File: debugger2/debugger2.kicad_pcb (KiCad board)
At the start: 2 copper layers, 65 x 30 mm, 63 parts, among them IC1 AT24CS32-SSHM, P1 CONN_01X01, P2 CONN_01X01, P3 USB_OTG, P4 CONN_02X20, P5 CONN_01X02, Q1 Q_PMOS_GSD, Q2 DMMT3906_Dual_PNP, U1 93LC56B, U2 MIC9409x_SC-70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

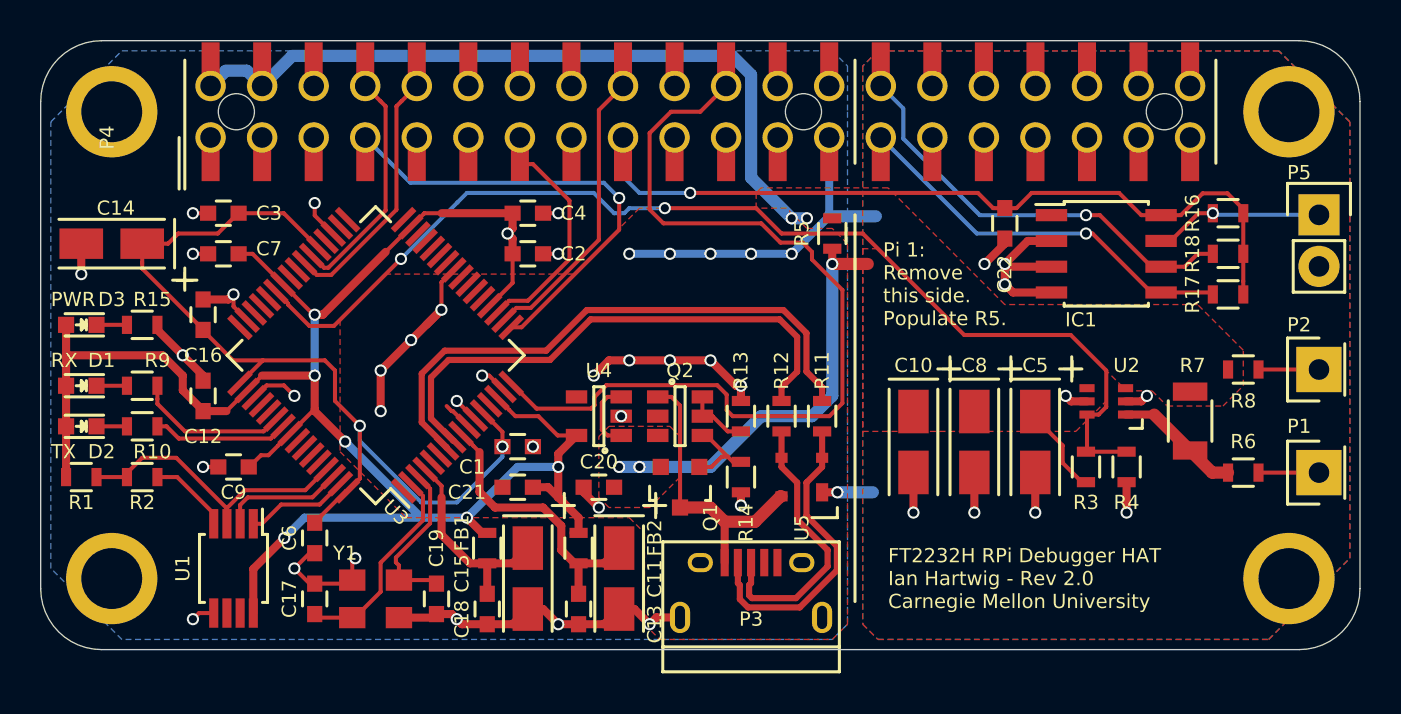
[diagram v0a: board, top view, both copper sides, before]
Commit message: rev 2.1 fixes for UART, JTAG resets, EEPROM packages
* fix UART (FTDI Ch B) RX/TX backwards
* fix GPIO22_TRST floating by connecting to FTDI Ch A. in debugger 1 we pulled up to 3.3V, but this gives us software control of tap reset
* add options to control RPi power (reset) from FTDI Ch A and button. diodes can be left off BOM to disable a source
* add external drain resistor for vbus switch (backpowering from rpi can cause fet drain in the switch to magic smoke)
* add grounding pad for probe clips
* make holes floating so we can use metal standoffs
* make FB1, FB2 be 0805 (not available in 0603)
* make both EEPROMs TSSOP for easier purchasing (but not compatible)
* reroute USB to a shorter path
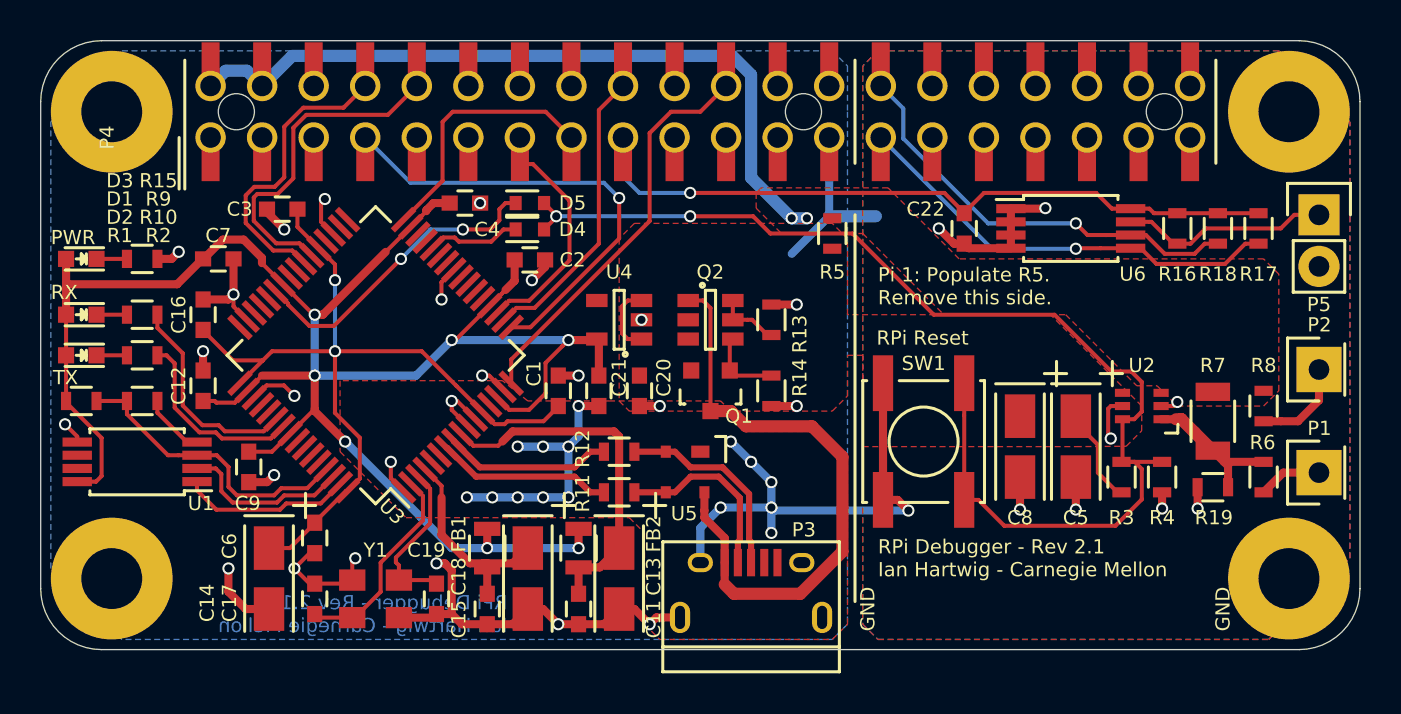
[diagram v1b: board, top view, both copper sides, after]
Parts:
- removed C10: 4.7u, Capacitors_Tantalum_SMD:TantalC_SizeA_EIA-3216_Wave
- removed IC1: AT24CS32-SSHM, Housings_SOIC:SOIC-8_3.9x4.9mm_Pitch1.27mm
- added D4: D_Small, Diodes_SMD:SOD-523, F.Cu at (144.1, 99.3)
- added D5: D_Small, Diodes_SMD:SOD-523, F.Cu at (144.1, 98.0)
- added R19: 10k, Resistors_SMD:R_0603, F.Cu at (177.8, 112.0)
- added SW1: SW_PUSH, Buttons_Switches_SMD:SW_SPST_EVPBF, F.Cu at (163.5, 109.8)
- added U6: AT24CS32-SSHM, Housings_SSOP:TSSOP-8_4.4x3mm_Pitch0.65mm, F.Cu at (170.8, 99.2)
- FB1, FB2: footprint Resistors_SMD:R_0603 -> Resistors_SMD:R_0805
- U1: footprint Housings_SSOP:MSOP-8_3x3mm_Pitch0.65mm -> Housings_SSOP:TSSOP-8_4.4x3mm_Pitch0.65mm
- moved C14 18.2 mm to (131.2, 116.5), turned to 270 degrees
- moved R11 10.7 mm to (148.5, 112.2), turned to 0 degrees
- moved R12 8.19 mm to (148.5, 110.2), turned to 0 degrees
- moved U1 7.08 mm to (124.8, 110.8), turned to 180 degrees
- moved C21 6.21 mm to (147.5, 107.2), turned to 270 degrees
- moved U5 5.76 mm to (151.8, 111.2), turned to 180 degrees
- moved C20 5.15 mm to (149.5, 107.2), turned to 270 degrees
- moved Q1 4.98 mm to (153.0, 107.2)
- moved Q2 4.98 mm to (153.0, 103.8)
- moved R13 4.98 mm to (156.0, 103.8)
- moved U4 4.85 mm to (148.5, 103.8)
- moved R14 4.51 mm to (156.0, 107.2)
- moved R1 3.75 mm to (122.0, 107.8)
- moved R2 3.75 mm to (125.0, 107.8)
- moved R17 3.58 mm to (180.0, 99.2), turned to 270 degrees
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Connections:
- H1 pad 1: GND -> (no net)
- H2 pad 1: GND -> (no net)
- H3 pad 1: GND -> (no net)
- H4 pad 1: GND -> (no net)
- U3 pad 28: (no net) -> /~JTAG_SRST
- U3 pad 32: (no net) -> /GPIO22_TRST
- U3 pad 38: /GPIO14_TXD0 -> /GPIO15_RXD0
- U3 pad 39: /GPIO15_RXD0 -> /GPIO14_TXD0
- U3 pad 43: /RPI_VBUS_EN -> /~UART_DTR
- U5 pad 2: /USB_D- -> /USB_D+
- U5 pad 3: /USB_D+ -> /USB_D-
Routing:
- net /GPIO25_TCK: track 45.6 -> 21.2 mm
- net /USB_VBUS: track 29.1 -> 8.28 mm, vias 3 -> 0
- net /FT_USB_D-: track 28.6 -> 8.66 mm
- net /FT_USB_D+: track 26.7 -> 8.28 mm
- net GND: track 113.0 -> 130.1 mm, vias 46 -> 49
- net /USB_VBUS_RVP: track 14.1 -> 30.2 mm
- net /~UART_DTR: track 0.00 -> 15.4 mm, vias 0 -> 2
- net /GPIO22_TRST: track 1.31 -> 14.0 mm
- net /USB_D-: track 15.3 -> 9.18 mm
- net /~JTAG_SRST: track 0.00 -> 4.66 mm
- net /RPI_3V3_2: track 40.2 -> 36.1 mm
- net /RPI_VBUS_EN: track 55.0 -> 58.9 mm
- net /USB_D+: track 13.8 -> 9.94 mm
- net /GPIO15_RXD0: track 13.9 -> 17.8 mm
- net +3V3: track 93.3 -> 97.1 mm
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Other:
- board text added: "GND"
- board text added: "Pi 1: Populate R5. Remove this side."
- board text added: "RPi Debugger - Rev 2.1 Ian Hartwig - Carnegie Mellon"
- board text added: "RPi Reset"
- board text removed: "FT2232H RPi Debugger HAT Ian Hartwig - Rev 2.0 Carnegie Mellon University"
- board text removed: "Pi 1: Remove this side. Populate R5."

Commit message: rev 2.1.1 swap usb micro b to SMT version since many board houses can't make the slots
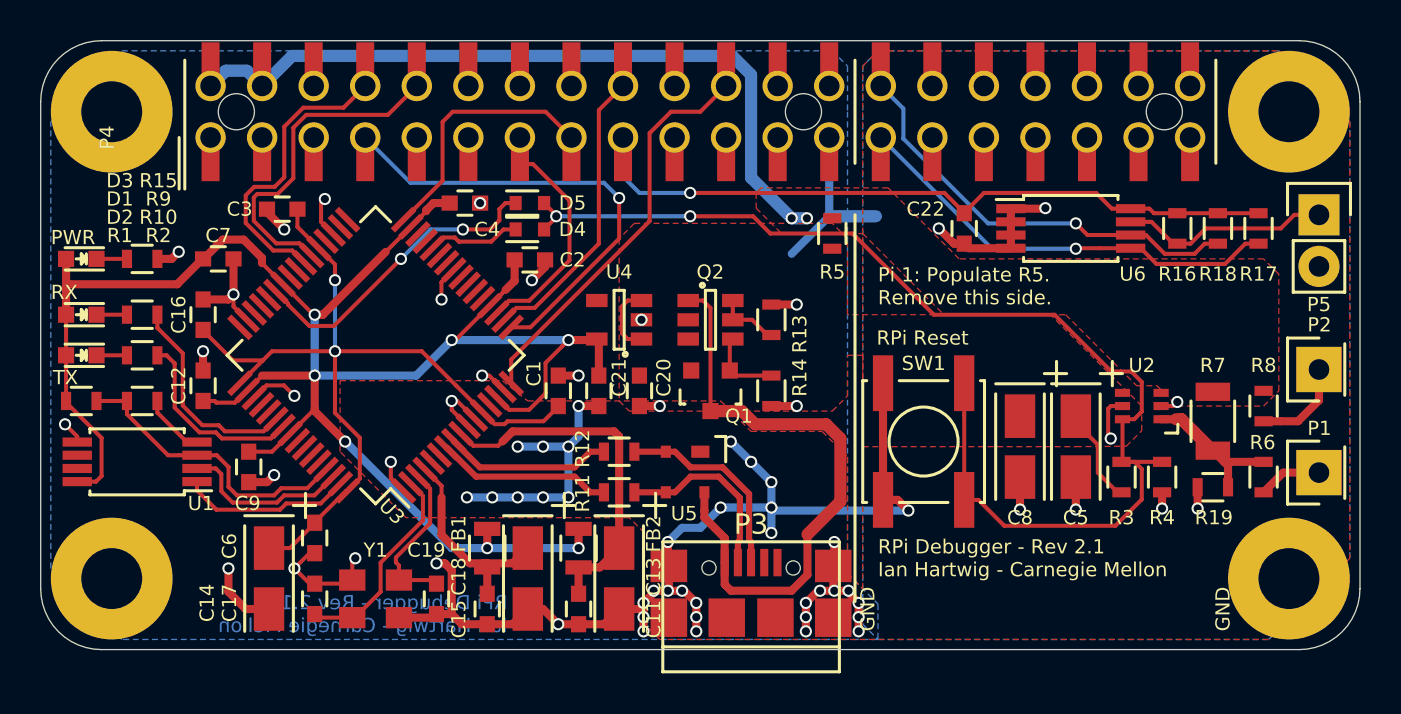
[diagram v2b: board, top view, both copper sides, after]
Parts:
- P3: footprint Connect:USB_Micro-B -> debugger2-special:USB_Micro-B_SMT
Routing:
- net GND: track 130.1 -> 144.8 mm, vias 49 -> 68

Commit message: rev 2.1.2 swap tantalum caps for ceramic, 2:1 aspect vias
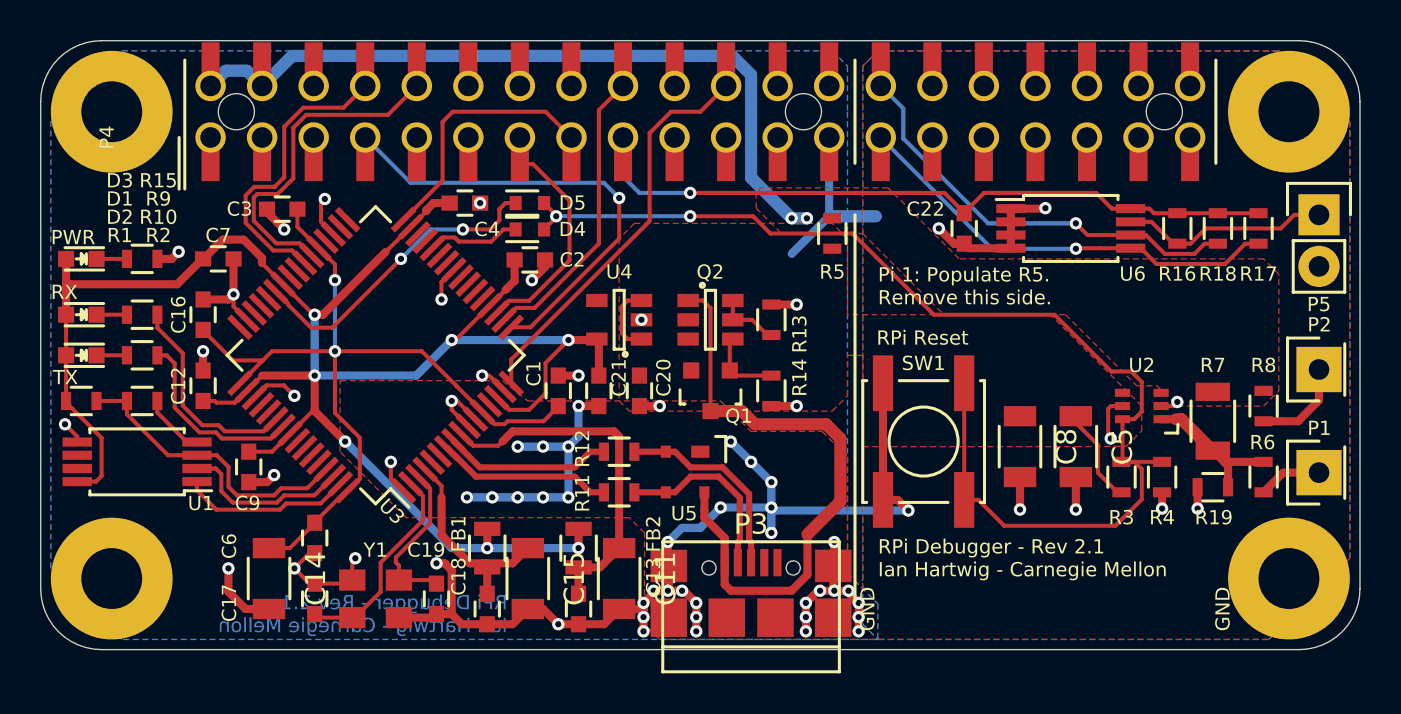
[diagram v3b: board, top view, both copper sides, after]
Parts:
- C11, C14, C15, C5, C8: footprint Capacitors_Tantalum_SMD:TantalC_SizeA_EIA-3216_Wave -> Capacitors_SMD:C_1206
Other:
- net class Default: via_dia 0.6 -> 0.6096; via_drill 0.4 -> 0.3048
- net class PiPower: via_dia 0.6 -> 0.6096; via_drill 0.4 -> 0.3048
- net class Power: via_dia 0.6 -> 0.6096; via_drill 0.4 -> 0.3048
- net class USB: via_dia 0.6 -> 0.6096; via_drill 0.4 -> 0.3048

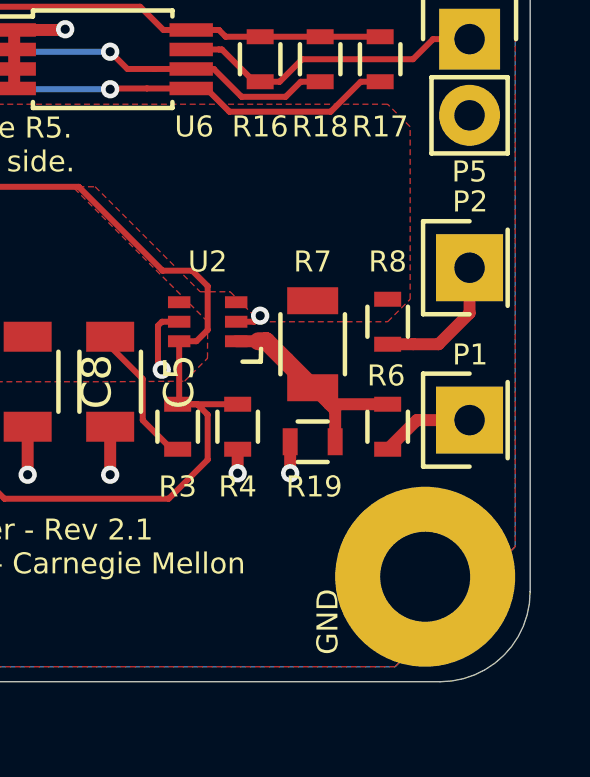
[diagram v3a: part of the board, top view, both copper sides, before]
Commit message: rev 2.1.3 combine P1 and P2, update BOM, make R3 possible value
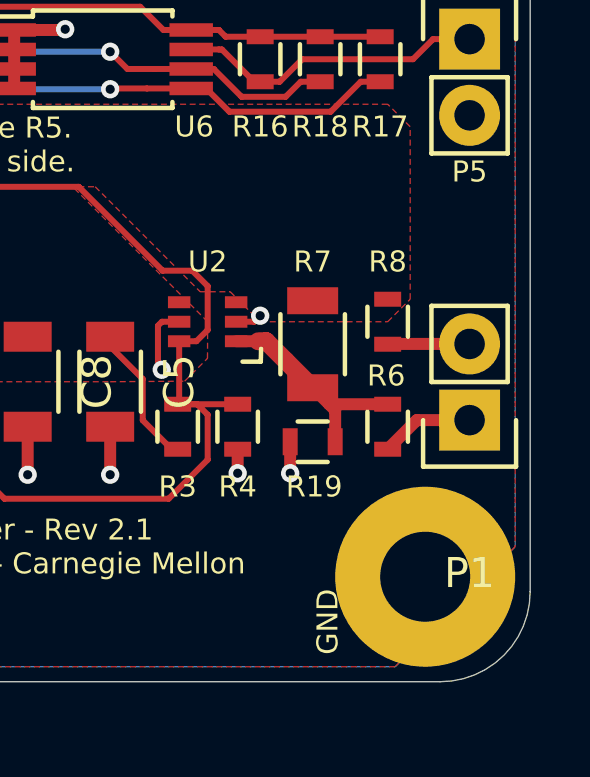
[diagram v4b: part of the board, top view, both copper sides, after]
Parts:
- removed P2: CONN_01X01, Pin_Headers:Pin_Header_Straight_1x01
- C22: value 100n -> dnp-100n
- P1: value CONN_01X01 -> CONN_01X02; footprint Pin_Headers:Pin_Header_Straight_1x01 -> Pin_Headers:Pin_Header_Straight_1x02
- P5: value CONN_01X02 -> dnp-CONN_01X02
- R16: value 1k -> dnp-1k
- R17, R18: value 3.9k -> dnp-3.9k
- R3: value 17k -> 20k
- R5: value DNP -> dnp-0
- U6: value AT24CS32-SSHM -> dnp-AT24CS32-SSHM
- turned P1 to 180 degrees
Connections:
- R8 pad 2: Net-(P2-Pad1) -> Net-(P1-Pad2)
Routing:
- net Net-(P2-Pad1): track 4.68 -> 0.00 mm
- net Net-(P1-Pad2): track 0.00 -> 2.73 mm

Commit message: swap rpi connector for no paste verison and no stuff
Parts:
- P4: value CONN_02X20 -> dnp-REF-182665-01; footprint debugger2-special:Pin_Header_Straight_TH-SMT_2x20 -> debugger2-special:Pin_Header_Straight_TH-SMT-NoPaste_2x20
- R7: value 0.01 -> 0.05
